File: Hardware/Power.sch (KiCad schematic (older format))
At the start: 20 parts, among them U8 LTC3129-SOP, U9 AOZ1280

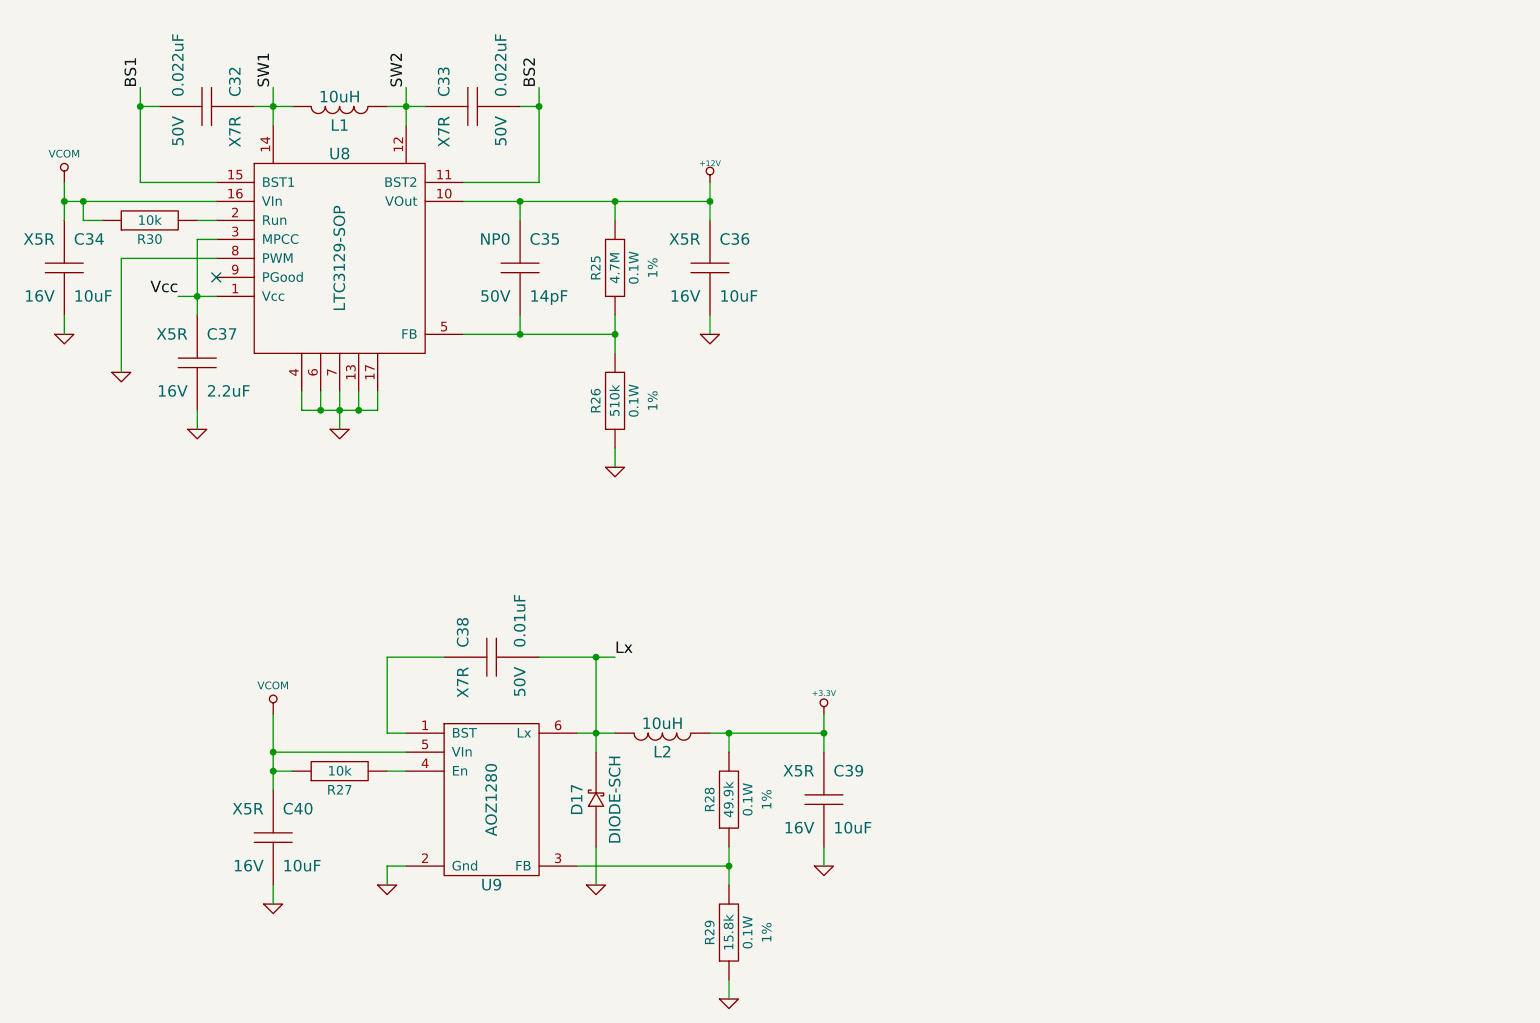
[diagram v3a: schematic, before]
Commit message: Move amplifiers into detection subsheets
Reannotate
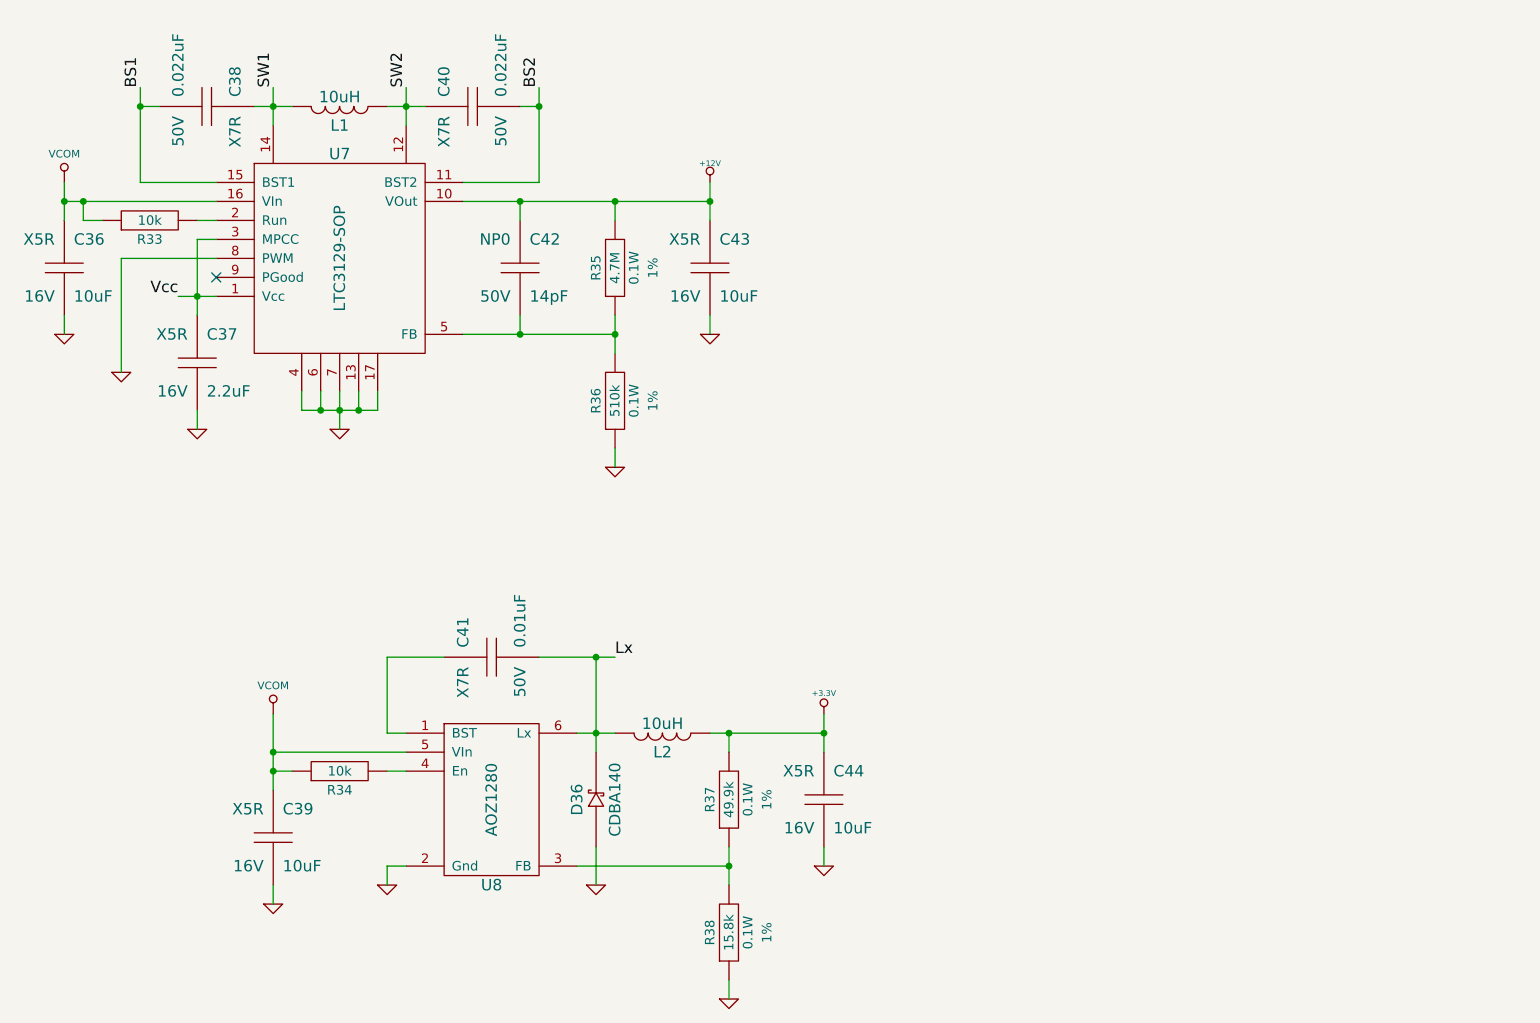
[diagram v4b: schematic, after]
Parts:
- D36: renamed from D17; value DIODE-SCH -> CDBA140
- renumbered C34 to C36, C32 to C38, C40 to C39, C33 to C40, C38 to C41, C35 to C42, C36 to C43, C39 to C44, R30 to R33, R27 to R34, R25 to R35, R26 to R36, R28 to R37, R29 to R38, U8 to U7, U9 to U8
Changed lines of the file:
@@
 $Descr A4 11693 8268
 encoding utf-8
-Sheet 8 7
+Sheet 5 5
 Title ""
 Date "24 dec 2013"
@@
 $EndDescr
 $Comp
-L VCOM #PWR88
+L VCOM #PWR84
 U 1 1 5241F463
 P 1300 2000
-F 0 "#PWR88" H 1300 2200 40  0001 C CNN
+F 0 "#PWR84" H 1300 2200 40  0001 C CNN
 F 1 "VCOM" H 1300 2150 40  0000 C CNN
 F 2 "" H 1300 2000 60  0000 C CNN
@@
 $EndComp
 $Comp
-L +12V #PWR087
+L +12V #PWR082
 U 1 1 5241F47C
 P 4700 2000
-F 0 "#PWR087" H 4700 1950 20  0001 C CNN
+F 0 "#PWR082" H 4700 1950 20  0001 C CNN
 F 1 "+12V" H 4700 2100 30  0000 C CNN
 F 2 "" H 4700 2000 60  0000 C CNN
@@
 $EndComp
 $Comp
-L +3.3V #PWR088
+L +3.3V #PWR083
 U 1 1 5241F48B
 P 5300 4800
-F 0 "#PWR088" H 5300 4760 30  0001 C CNN
+F 0 "#PWR083" H 5300 4760 30  0001 C CNN
 F 1 "+3.3V" H 5300 4910 30  0000 C CNN
 F 2 "" H 5300 4800 60  0000 C CNN
@@
 $EndComp
 $Comp
-L C C32
+L C C38
 U 1 1 52450BC1
 P 2050 1600
-F 0 "C32" H 2100 1750 60  0000 L CNN
+F 0 "C38" H 2100 1750 60  0000 L CNN
 F 1 "0.022uF" H 2100 1450 60  0000 L CNN
 F 2 "~" H 2050 1600 60  0000 C CNN
@@
 $EndComp
 $Comp
-L R R25
+L R R35
 U 1 1 52450D6B
 P 4200 2450
-F 0 "R25" H 4200 2550 50  0000 C CNN
+F 0 "R35" H 4200 2550 50  0000 C CNN
 F 1 "4.7M" H 4200 2450 50  0000 C CNN
 F 2 "~" H 4200 2450 60  0000 C CNN
@@
 $EndComp
 $Comp
-L C C35
+L C C42
 U 1 1 52450D94
 P 3700 2450
-F 0 "C35" H 3750 2600 60  0000 L CNN
+F 0 "C42" H 3750 2600 60  0000 L CNN
 F 1 "14pF" H 3750 2300 60  0000 L CNN
 F 2 "~" H 3700 2450 60  0000 C CNN
@@
 $EndComp
 $Comp
-L R R26
+L R R36
 U 1 1 52450DD8
 P 4200 3150
-F 0 "R26" H 4200 3250 50  0000 C CNN
+F 0 "R36" H 4200 3250 50  0000 C CNN
 F 1 "510k" H 4200 3150 50  0000 C CNN
 F 2 "~" H 4200 3150 60  0000 C CNN
@@
 $EndComp
 $Comp
-L C C36
+L C C43
 U 1 1 52450DF3
 P 4700 2450
-F 0 "C36" H 4750 2600 60  0000 L CNN
+F 0 "C43" H 4750 2600 60  0000 L CNN
 F 1 "10uF" H 4750 2300 60  0000 L CNN
 F 2 "~" H 4700 2450 60  0000 C CNN
@@
 $EndComp
 $Comp
-L LTC3129-SOP U8
+L LTC3129-SOP U7
 U 1 1 52451268
 P 2750 2400
-F 0 "U8" H 2750 2950 60  0000 C CNN
+F 0 "U7" H 2750 2950 60  0000 C CNN
 F 1 "LTC3129-SOP" V 2750 2400 60  0000 C CNN
 F 2 "" H 2750 2300 60  0000 C CNN
@@
 NoConn ~ 2100 2500
 $Comp
-L GND #PWR089
+L GND #PWR084
 U 1 1 52451996
 P 2750 3300
-F 0 "#PWR089" H 2750 3300 30  0001 C CNN
+F 0 "#PWR084" H 2750 3300 30  0001 C CNN
 F 1 "GND" H 2750 3230 30  0001 C CNN
 F 2 "" H 2750 3300 60  0000 C CNN
@@
 Connection ~ 2850 3200
 $Comp
-L GND #PWR090
+L GND #PWR085
 U 1 1 52451A61
 P 1300 2800
-F 0 "#PWR090" H 1300 2800 30  0001 C CNN
+F 0 "#PWR085" H 1300 2800 30  0001 C CNN
 F 1 "GND" H 1300 2730 30  0001 C CNN
 F 2 "" H 1300 2800 60  0000 C CNN
@@
 $EndComp
 $Comp
-L GND #PWR091
+L GND #PWR086
 U 1 1 52451A70
 P 2000 3300
-F 0 "#PWR091" H 2000 3300 30  0001 C CNN
+F 0 "#PWR086" H 2000 3300 30  0001 C CNN
 F 1 "GND" H 2000 3230 30  0001 C CNN
 F 2 "" H 2000 3300 60  0000 C CNN
@@
 $EndComp
 $Comp
-L GND #PWR092
+L GND #PWR087
 U 1 1 52451A7F
 P 4200 3500
-F 0 "#PWR092" H 4200 3500 30  0001 C CNN
+F 0 "#PWR087" H 4200 3500 30  0001 C CNN
 F 1 "GND" H 4200 3430 30  0001 C CNN
 F 2 "" H 4200 3500 60  0000 C CNN
@@
 $EndComp
 $Comp
-L GND #PWR093
+L GND #PWR088
 U 1 1 52451A8E
 P 4700 2800
-F 0 "#PWR093" H 4700 2800 30  0001 C CNN
+F 0 "#PWR088" H 4700 2800 30  0001 C CNN
 F 1 "GND" H 4700 2730 30  0001 C CNN
 F 2 "" H 4700 2800 60  0000 C CNN
@@
 $EndComp
 $Comp
-L GND #PWR094
+L GND #PWR089
 U 1 1 52451A9D
 P 1600 3000
-F 0 "#PWR094" H 1600 3000 30  0001 C CNN
+F 0 "#PWR089" H 1600 3000 30  0001 C CNN
 F 1 "GND" H 1600 2930 30  0001 C CNN
 F 2 "" H 1600 3000 60  0000 C CNN
@@
 Connection ~ 4700 2100
 $Comp
-L C C34
+L C C36
 U 1 1 52453F18
 P 1300 2450
-F 0 "C34" H 1350 2600 60  0000 L CNN
+F 0 "C36" H 1350 2600 60  0000 L CNN
 F 1 "10uF" H 1350 2300 60  0000 L CNN
 F 2 "~" H 1300 2450 60  0000 C CNN
@@
 $EndComp
 $Comp
-L C C33
+L C C40
 U 1 1 5245417C
 P 3450 1600
-F 0 "C33" H 3500 1750 60  0000 L CNN
+F 0 "C40" H 3500 1750 60  0000 L CNN
 F 1 "0.022uF" H 3500 1450 60  0000 L CNN
 F 2 "~" H 3450 1600 60  0000 C CNN
@@
 Connection ~ 1700 1600
 $Comp
-L VCOM #PWR96
+L VCOM #PWR88
 U 1 1 52455206
 P 2400 4800
-F 0 "#PWR96" H 2400 5000 40  0001 C CNN
+F 0 "#PWR88" H 2400 5000 40  0001 C CNN
 F 1 "VCOM" H 2400 4950 40  0000 C CNN
 F 2 "" H 2400 4800 60  0000 C CNN
@@
 $EndComp
 $Comp
-L AOZ1280 U9
+L AOZ1280 U8
 U 1 1 52455ED9
 P 3550 5250
-F 0 "U9" H 3550 4800 60  0000 C CNN
+F 0 "U8" H 3550 4800 60  0000 C CNN
 F 1 "AOZ1280" V 3550 5250 60  0000 C CNN
 F 2 "" H 3550 5600 60  0000 C CNN
@@
 $EndComp
 $Comp
-L DIODE-SCH D17
+L DIODE-SCH D36
 U 1 1 52455EF2
 P 4100 5250
-F 0 "D17" H 4100 5350 60  0000 C CNN
-F 1 "DIODE-SCH" H 4100 5150 60  0000 C CNN
+F 0 "D36" H 4100 5350 60  0000 C CNN
+F 1 "CDBA140" H 4100 5150 60  0000 C CNN
 F 2 "~" H 4100 5250 60  0000 C CNN
 F 3 "~" H 4100 5250 60  0000 C CNN
@@
 $EndComp
 $Comp
-L R R28
+L R R37
 U 1 1 52455F0B
 P 4800 5250
-F 0 "R28" H 4800 5350 50  0000 C CNN
+F 0 "R37" H 4800 5350 50  0000 C CNN
 F 1 "49.9k" H 4800 5250 50  0000 C CNN
 F 2 "RESC1608" H 4800 5250 60  0001 C CNN
@@
 $EndComp
 $Comp
-L R R29
+L R R38
 U 1 1 52455F41
 P 4800 5950
-F 0 "R29" H 4800 6050 50  0000 C CNN
+F 0 "R38" H 4800 6050 50  0000 C CNN
 F 1 "15.8k" H 4800 5950 50  0000 C CNN
 F 2 "RESC1608" H 4800 5950 60  0001 C CNN
@@
 Connection ~ 4800 5600
 $Comp
-L R R27
+L R R34
 U 1 1 52456166
 P 2750 5100
-F 0 "R27" H 2750 5200 50  0000 C CNN
+F 0 "R34" H 2750 5200 50  0000 C CNN
 F 1 "10k" H 2750 5100 50  0000 C CNN
 F 2 "~" H 2750 5100 60  0000 C CNN
@@
 	3000 5100 3100 5100
 $Comp
-L GND #PWR095
+L GND #PWR090
 U 1 1 5245631B
 P 2400 5800
-F 0 "#PWR095" H 2400 5800 30  0001 C CNN
+F 0 "#PWR090" H 2400 5800 30  0001 C CNN
 F 1 "GND" H 2400 5730 30  0001 C CNN
 F 2 "" H 2400 5800 60  0000 C CNN
@@
 $EndComp
 $Comp
-L GND #PWR096
+L GND #PWR091
 U 1 1 5245632A
 P 3000 5700
-F 0 "#PWR096" H 3000 5700 30  0001 C CNN
+F 0 "#PWR091" H 3000 5700 30  0001 C CNN
 F 1 "GND" H 3000 5630 30  0001 C CNN
 F 2 "" H 3000 5700 60  0000 C CNN
@@
 $EndComp
 $Comp
-L GND #PWR097
+L GND #PWR092
 U 1 1 52456339
 P 5300 5600
-F 0 "#PWR097" H 5300 5600 30  0001 C CNN
+F 0 "#PWR092" H 5300 5600 30  0001 C CNN
 F 1 "GND" H 5300 5530 30  0001 C CNN
 F 2 "" H 5300 5600 60  0000 C CNN
@@
 $EndComp
 $Comp
-L GND #PWR098
+L GND #PWR093
 U 1 1 52456348
 P 4800 6300
-F 0 "#PWR098" H 4800 6300 30  0001 C CNN
+F 0 "#PWR093" H 4800 6300 30  0001 C CNN
 F 1 "GND" H 4800 6230 30  0001 C CNN
 F 2 "" H 4800 6300 60  0000 C CNN
@@
 $EndComp
 $Comp
-L GND #PWR099
+L GND #PWR094
 U 1 1 52456357
 P 4100 5700
-F 0 "#PWR099" H 4100 5700 30  0001 C CNN
+F 0 "#PWR094" H 4100 5700 30  0001 C CNN
 F 1 "GND" H 4100 5630 30  0001 C CNN
 F 2 "" H 4100 5700 60  0000 C CNN
@@
 $EndComp
 $Comp
-L C C40
+L C C39
 U 1 1 52456A9F
 P 2400 5450
-F 0 "C40" H 2450 5600 60  0000 L CNN
+F 0 "C39" H 2450 5600 60  0000 L CNN
 F 1 "10uF" H 2450 5300 60  0000 L CNN
 F 2 "~" H 2400 5450 60  0000 C CNN
@@
 Connection ~ 4100 4500
 $Comp
-L C C38
+L C C41
 U 1 1 52457190
 P 3550 4500
-F 0 "C38" H 3600 4650 60  0000 L CNN
+F 0 "C41" H 3600 4650 60  0000 L CNN
 F 1 "0.01uF" H 3600 4350 60  0000 L CNN
 F 2 "CAPC1608" H 3550 4500 60  0001 C CNN
@@
 $EndComp
 $Comp
-L C C39
+L C C44
 U 1 1 5245816D
 P 5300 5250
-F 0 "C39" H 5350 5400 60  0000 L CNN
+F 0 "C44" H 5350 5400 60  0000 L CNN
 F 1 "10uF" H 5350 5100 60  0000 L CNN
 F 2 "~" H 5300 5250 60  0000 C CNN
@@
 	2100 2100 1300 2100
 $Comp
-L R R30
+L R R33
 U 1 1 52A3E59A
 P 1750 2200
-F 0 "R30" H 1750 2300 50  0000 C CNN
+F 0 "R33" H 1750 2300 50  0000 C CNN
 F 1 "10k" H 1750 2200 50  0000 C CNN
 F 2 "~" H 1750 2200 60  0000 C CNN

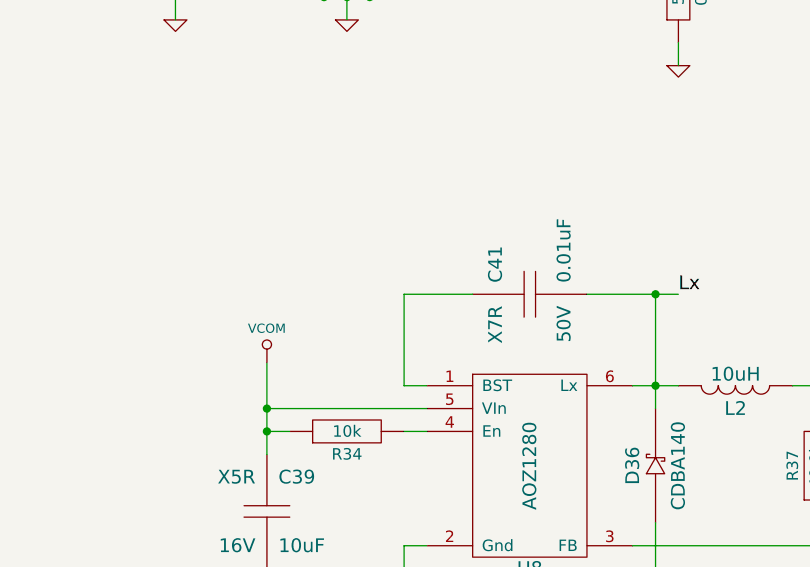
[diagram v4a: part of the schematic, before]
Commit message: New signal chain layout
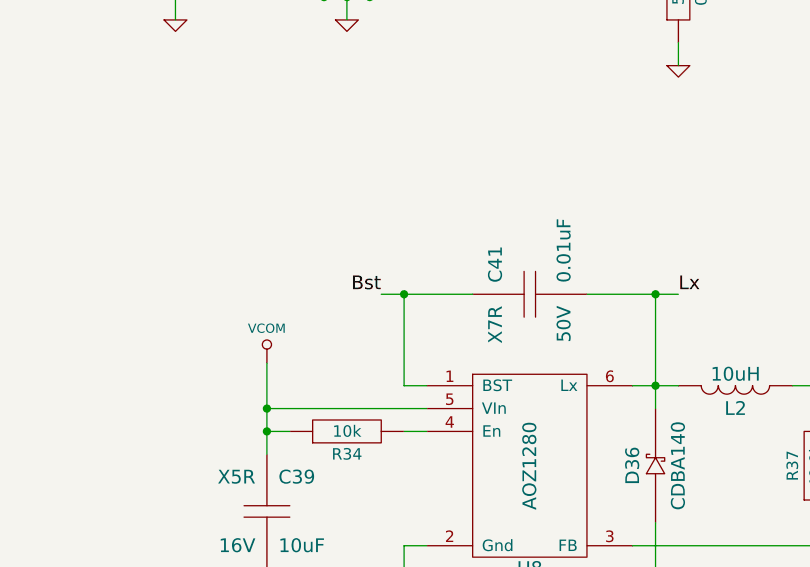
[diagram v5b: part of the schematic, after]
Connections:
- net Bst: now reaches C41.1, U8.1 (BST)
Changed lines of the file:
@@
 Sheet 5 5
 Title ""
-Date "24 dec 2013"
+Date "26 dec 2013"
 Rev ""
 Comp ""
@@
 $EndComp
 $Comp
-L +12V #PWR082
+L +12V #PWR083
 U 1 1 5241F47C
 P 4700 2000
-F 0 "#PWR082" H 4700 1950 20  0001 C CNN
+F 0 "#PWR083" H 4700 1950 20  0001 C CNN
 F 1 "+12V" H 4700 2100 30  0000 C CNN
 F 2 "" H 4700 2000 60  0000 C CNN
@@
 $EndComp
 $Comp
-L +3.3V #PWR083
+L +3.3V #PWR084
 U 1 1 5241F48B
 P 5300 4800
-F 0 "#PWR083" H 5300 4760 30  0001 C CNN
+F 0 "#PWR084" H 5300 4760 30  0001 C CNN
 F 1 "+3.3V" H 5300 4910 30  0000 C CNN
 F 2 "" H 5300 4800 60  0000 C CNN
@@
 NoConn ~ 2100 2500
 $Comp
-L GND #PWR084
+L GND #PWR085
 U 1 1 52451996
 P 2750 3300
-F 0 "#PWR084" H 2750 3300 30  0001 C CNN
+F 0 "#PWR085" H 2750 3300 30  0001 C CNN
 F 1 "GND" H 2750 3230 30  0001 C CNN
 F 2 "" H 2750 3300 60  0000 C CNN
@@
 Connection ~ 2850 3200
 $Comp
-L GND #PWR085
+L GND #PWR086
 U 1 1 52451A61
 P 1300 2800
-F 0 "#PWR085" H 1300 2800 30  0001 C CNN
+F 0 "#PWR086" H 1300 2800 30  0001 C CNN
 F 1 "GND" H 1300 2730 30  0001 C CNN
 F 2 "" H 1300 2800 60  0000 C CNN
@@
 $EndComp
 $Comp
-L GND #PWR086
+L GND #PWR087
 U 1 1 52451A70
 P 2000 3300
-F 0 "#PWR086" H 2000 3300 30  0001 C CNN
+F 0 "#PWR087" H 2000 3300 30  0001 C CNN
 F 1 "GND" H 2000 3230 30  0001 C CNN
 F 2 "" H 2000 3300 60  0000 C CNN
@@
 $EndComp
 $Comp
-L GND #PWR087
+L GND #PWR088
 U 1 1 52451A7F
 P 4200 3500
-F 0 "#PWR087" H 4200 3500 30  0001 C CNN
+F 0 "#PWR088" H 4200 3500 30  0001 C CNN
 F 1 "GND" H 4200 3430 30  0001 C CNN
 F 2 "" H 4200 3500 60  0000 C CNN
@@
 $EndComp
 $Comp
-L GND #PWR088
+L GND #PWR089
 U 1 1 52451A8E
 P 4700 2800
-F 0 "#PWR088" H 4700 2800 30  0001 C CNN
+F 0 "#PWR089" H 4700 2800 30  0001 C CNN
 F 1 "GND" H 4700 2730 30  0001 C CNN
 F 2 "" H 4700 2800 60  0000 C CNN
@@
 $EndComp
 $Comp
-L GND #PWR089
+L GND #PWR090
 U 1 1 52451A9D
 P 1600 3000
-F 0 "#PWR089" H 1600 3000 30  0001 C CNN
+F 0 "#PWR090" H 1600 3000 30  0001 C CNN
 F 1 "GND" H 1600 2930 30  0001 C CNN
 F 2 "" H 1600 3000 60  0000 C CNN
@@
 	3000 4900 3000 4500
 Wire Wire Line
-	3000 4500 3300 4500
+	2900 4500 3300 4500
 Wire Wire Line
 	4000 4900 4200 4900
@@
 	3000 5100 3100 5100
 $Comp
-L GND #PWR090
+L GND #PWR091
 U 1 1 5245631B
 P 2400 5800
-F 0 "#PWR090" H 2400 5800 30  0001 C CNN
+F 0 "#PWR091" H 2400 5800 30  0001 C CNN
 F 1 "GND" H 2400 5730 30  0001 C CNN
 F 2 "" H 2400 5800 60  0000 C CNN
@@
 $EndComp
 $Comp
-L GND #PWR091
+L GND #PWR092
 U 1 1 5245632A
 P 3000 5700
-F 0 "#PWR091" H 3000 5700 30  0001 C CNN
+F 0 "#PWR092" H 3000 5700 30  0001 C CNN
 F 1 "GND" H 3000 5630 30  0001 C CNN
 F 2 "" H 3000 5700 60  0000 C CNN
@@
 $EndComp
 $Comp
-L GND #PWR092
+L GND #PWR093
 U 1 1 52456339
 P 5300 5600
-F 0 "#PWR092" H 5300 5600 30  0001 C CNN
+F 0 "#PWR093" H 5300 5600 30  0001 C CNN
 F 1 "GND" H 5300 5530 30  0001 C CNN
 F 2 "" H 5300 5600 60  0000 C CNN
@@
 $EndComp
 $Comp
-L GND #PWR093
+L GND #PWR094
 U 1 1 52456348
 P 4800 6300
-F 0 "#PWR093" H 4800 6300 30  0001 C CNN
+F 0 "#PWR094" H 4800 6300 30  0001 C CNN
 F 1 "GND" H 4800 6230 30  0001 C CNN
 F 2 "" H 4800 6300 60  0000 C CNN
@@
 $EndComp
 $Comp
-L GND #PWR094
+L GND #PWR095
 U 1 1 52456357
 P 4100 5700
-F 0 "#PWR094" H 4100 5700 30  0001 C CNN
+F 0 "#PWR095" H 4100 5700 30  0001 C CNN
 F 1 "GND" H 4100 5630 30  0001 C CNN
 F 2 "" H 4100 5700 60  0000 C CNN
@@
 Text Label 1900 2600 2    60   ~ 0
 Vcc
+Text Label 2900 4500 2    60   ~ 0
+Bst
+Connection ~ 3000 4500
 $EndSCHEMATC
